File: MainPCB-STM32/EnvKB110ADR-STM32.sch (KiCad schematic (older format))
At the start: 246 parts, among them SW1 Boot Mode, SW2 Reset Switch, U1 XC6206PxxxMR, U2 STM32F411CEUx, Y1 3225_4P 32.768khz

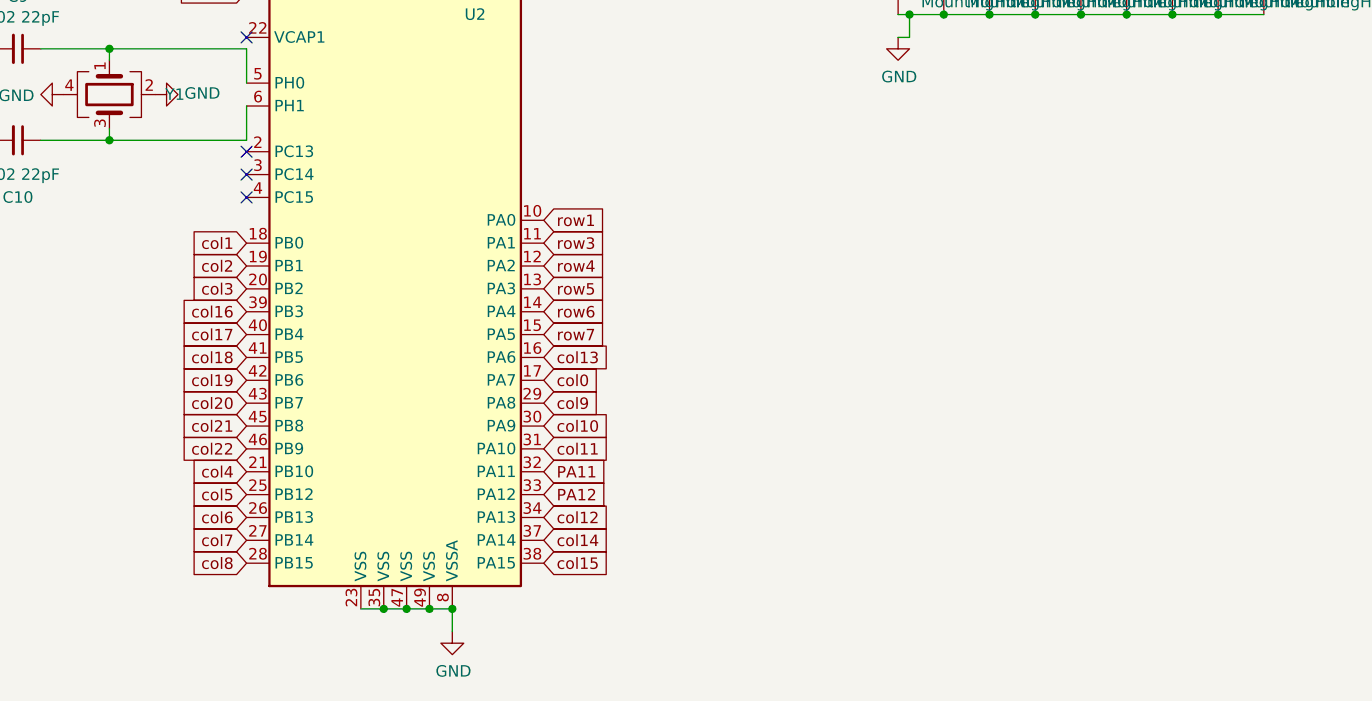
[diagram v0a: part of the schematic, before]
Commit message: Flipped STM32 to other side of board and added a debug header (SWDIO/SWCLK)
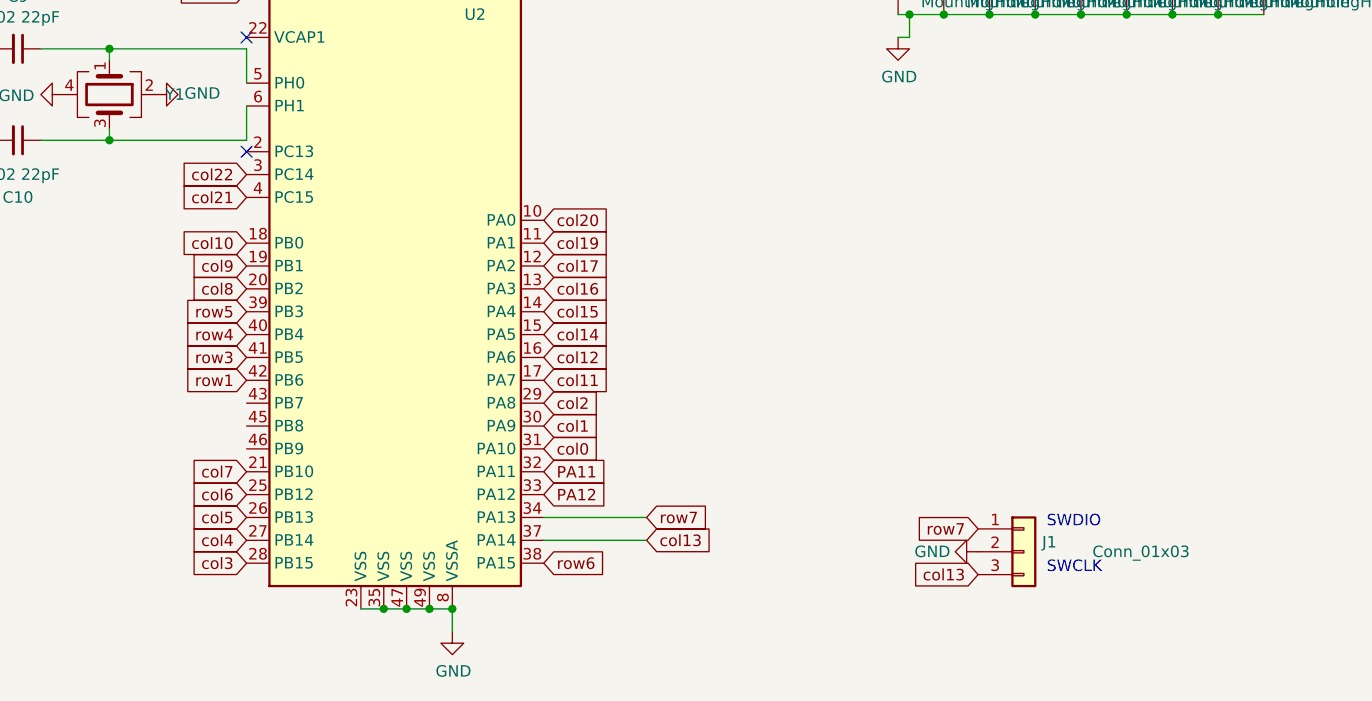
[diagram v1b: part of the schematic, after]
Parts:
- added J1: Conn_01x03, Connector_PinSocket_2.54mm:PinSocket_1x03_P2.54mm_Horizontal, symbol Connector_Generic:Conn_01x03
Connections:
- net col18 is gone; now on net row3: U2.41 (PB5)
- net GND: now also J1.2 (Pin_2)
- net col0: now also U2.31 (PA10); no longer U2.17 (PA7)
- net col1: now also U2.30 (PA9); no longer U2.18 (PB0)
- net col10: now also U2.18 (PB0); no longer U2.30 (PA9)
- net col11: now also U2.17 (PA7); no longer U2.31 (PA10)
- net col12: now also U2.16 (PA6); no longer U2.34 (PA13)
- net col13: now also U2.37 (PA14), J1.3 (Pin_3); no longer U2.16 (PA6)
- net col14: now also U2.15 (PA5); no longer U2.37 (PA14)
- net col15: now also U2.14 (PA4); no longer U2.38 (PA15)
- net col16: now also U2.13 (PA3); no longer U2.39 (PB3)
- net col17: now also U2.12 (PA2); no longer U2.40 (PB4)
- net col19: now also U2.11 (PA1); no longer U2.42 (PB6)
- net col2: now also U2.29 (PA8); no longer U2.19 (PB1)
- net col20: now also U2.10 (PA0); no longer U2.43 (PB7)
- net col21: now also U2.4 (PC15); no longer U2.45 (PB8)
- net col22: now also U2.3 (PC14); no longer U2.46 (PB9)
- net col3: now also U2.28 (PB15); no longer U2.20 (PB2)
- net col4: now also U2.27 (PB14); no longer U2.21 (PB10)
- net col5: now also U2.26 (PB13); no longer U2.25 (PB12)
- net col6: now also U2.25 (PB12); no longer U2.26 (PB13)
- net col7: now also U2.21 (PB10); no longer U2.27 (PB14)
- net col8: now also U2.20 (PB2); no longer U2.28 (PB15)
- net col9: now also U2.19 (PB1); no longer U2.29 (PA8)
- net row1: now also U2.42 (PB6); no longer U2.10 (PA0)
- net row3: no longer U2.11 (PA1)
- net row4: now also U2.40 (PB4); no longer U2.12 (PA2)
- net row5: now also U2.39 (PB3); no longer U2.13 (PA3)
- net row6: now also U2.38 (PA15); no longer U2.14 (PA4)
- net row7: now also U2.34 (PA13), J1.1 (Pin_1); no longer U2.15 (PA5)
- no-connect marks 7 -> 5
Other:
- note added: "SWCLK"
- note added: "SWDIO"
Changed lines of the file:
@@
 	1    0    0    -1
 $EndComp
+Text GLabel 14000 12250 2    50   Input ~ 0
+col0
+Text GLabel 14000 12150 2    50   Input ~ 0
+col1
+Text GLabel 14000 12050 2    50   Input ~ 0
+col2
+Text GLabel 12700 12750 0    50   Input ~ 0
+col3
+Text GLabel 12700 12650 0    50   Input ~ 0
+col4
+Text GLabel 12700 12550 0    50   Input ~ 0
+col5
+Text GLabel 12700 12450 0    50   Input ~ 0
+col6
+Text GLabel 12700 12350 0    50   Input ~ 0
+col7
+Text GLabel 12700 11550 0    50   Input ~ 0
+col8
+Text GLabel 12700 11450 0    50   Input ~ 0
+col9
+Text GLabel 12700 11350 0    50   Input ~ 0
+col10
 Text GLabel 14000 11950 2    50   Input ~ 0
-col0
-Text GLabel 12700 11350 0    50   Input ~ 0
-col1
-Text GLabel 12700 11450 0    50   Input ~ 0
-col2
-Text GLabel 12700 11550 0    50   Input ~ 0
-col3
-Text GLabel 12700 12350 0    50   Input ~ 0
-col4
-Text GLabel 12700 12450 0    50   Input ~ 0
-col5
-Text GLabel 12700 12550 0    50   Input ~ 0
-col6
-Text GLabel 12700 12650 0    50   Input ~ 0
-col7
-Text GLabel 12700 12750 0    50   Input ~ 0
-col8
-Text GLabel 14000 12050 2    50   Input ~ 0
-col9
-Text GLabel 14000 12150 2    50   Input ~ 0
-col10
-Text GLabel 14000 12250 2    50   Input ~ 0
 col11
-Text GLabel 14000 12550 2    50   Input ~ 0
+Text GLabel 14000 11850 2    50   Input ~ 0
 col12
-Text GLabel 14000 11850 2    50   Input ~ 0
+Text GLabel 14450 12650 2    50   Input ~ 0
 col13
-Text GLabel 14000 12650 2    50   Input ~ 0
+Text GLabel 14000 11750 2    50   Input ~ 0
 col14
+Text GLabel 14000 11650 2    50   Input ~ 0
+col15
+Text GLabel 14000 11550 2    50   Input ~ 0
+col16
+Text GLabel 14000 11450 2    50   Input ~ 0
+col17
+Text GLabel 14000 11350 2    50   Input ~ 0
+col19
+Text GLabel 14000 11250 2    50   Input ~ 0
+col20
+Text GLabel 12700 11150 0    50   Input ~ 0
+col21
+Text GLabel 12700 11050 0    50   Input ~ 0
+col22
+Text GLabel 12700 11950 0    50   Input ~ 0
+row1
+Text GLabel 12700 11850 0    50   Input ~ 0
+row3
+Text GLabel 12700 11750 0    50   Input ~ 0
+row4
+Text GLabel 12700 11650 0    50   Input ~ 0
+row5
 Text GLabel 14000 12750 2    50   Input ~ 0
-col15
-Text GLabel 12700 11650 0    50   Input ~ 0
-col16
-Text GLabel 12700 11750 0    50   Input ~ 0
-col17
-Text GLabel 12700 11850 0    50   Input ~ 0
-col18
-Text GLabel 12700 11950 0    50   Input ~ 0
-col19
-Text GLabel 12700 12050 0    50   Input ~ 0
-col20
-Text GLabel 12700 12150 0    50   Input ~ 0
-col21
-Text GLabel 12700 12250 0    50   Input ~ 0
-col22
-Text GLabel 14000 11250 2    50   Input ~ 0
-row1
-Text GLabel 14000 11350 2    50   Input ~ 0
-row3
-Text GLabel 14000 11450 2    50   Input ~ 0
-row4
-Text GLabel 14000 11550 2    50   Input ~ 0
-row5
-Text GLabel 14000 11650 2    50   Input ~ 0
 row6
-Text GLabel 14000 11750 2    50   Input ~ 0
+Text GLabel 14450 12550 2    50   Input ~ 0
 row7
 Wire Wire Line
@@
 Connection ~ 12100 10500
 $Comp
+L Device:C_Small C9
+U 1 1 616BF174
+P 11700 10500
+F 0 "C9" V 11929 10500 50  0000 C CNN
+F 1 "0402 22pF" V 11838 10500 50  0000 C CNN
+F 2 "Capacitor_SMD:C_0402_1005Metric" H 11700 10500 50  0001 C CNN
+F 3 "~" H 11700 10500 50  0001 C CNN
+	1    11700 10500
+	0    1    -1   0
+$EndComp
+$Comp
+L power:GND #PWR0118
+U 1 1 616C0646
+P 11900 10700
+F 0 "#PWR0118" H 11900 10450 50  0001 C CNN
+F 1 "GND" V 11905 10572 50  0000 R CNN
+F 2 "" H 11900 10700 50  0001 C CNN
+F 3 "" H 11900 10700 50  0001 C CNN
+	1    11900 10700
+	0    1    1    0
+$EndComp
+$Comp
+L power:GND #PWR0119
+U 1 1 616C18A1
+P 12300 10700
+F 0 "#PWR0119" H 12300 10450 50  0001 C CNN
+F 1 "GND" V 12305 10572 50  0000 R CNN
+F 2 "" H 12300 10700 50  0001 C CNN
+F 3 "" H 12300 10700 50  0001 C CNN
+	1    12300 10700
+	0    -1   -1   0
+$EndComp
+$Comp
+L power:GND #PWR0120
+U 1 1 616C1C2C
+P 11500 10700
+F 0 "#PWR0120" H 11500 10450 50  0001 C CNN
+F 1 "GND" V 11505 10572 50  0000 R CNN
+F 2 "" H 11500 10700 50  0001 C CNN
+F 3 "" H 11500 10700 50  0001 C CNN
+	1    11500 10700
+	0    1    1    0
+$EndComp
+Wire Wire Line
+	12700 10900 12100 10900
+Wire Wire Line
+	12100 10900 12100 10850
+Wire Wire Line
+	12100 10900 11800 10900
+Connection ~ 12100 10900
+Wire Wire Line
+	12700 10750 12700 10900
+Wire Wire Line
+	11600 10900 11600 10700
+Wire Wire Line
+	11600 10700 11500 10700
+Wire Wire Line
+	11600 10700 11600 10500
+Connection ~ 11600 10700
+NoConn ~ 12700 10950
+NoConn ~ 9550 11150
+NoConn ~ 9550 10550
+Wire Wire Line
+	9550 11450 9550 11550
+Connection ~ 9550 11550
+Wire Wire Line
+	9550 11550 9550 11650
+$Comp
 L Device:C_Small C10
 U 1 1 616BE7BD
@@
 	0    1    -1   0
 $EndComp
-$Comp
-L Device:C_Small C9
-U 1 1 616BF174
-P 11700 10500
-F 0 "C9" V 11929 10500 50  0000 C CNN
-F 1 "0402 22pF" V 11838 10500 50  0000 C CNN
-F 2 "Capacitor_SMD:C_0402_1005Metric" H 11700 10500 50  0001 C CNN
-F 3 "~" H 11700 10500 50  0001 C CNN
-	1    11700 10500
-	0    1    -1   0
-$EndComp
-$Comp
-L power:GND #PWR0118
-U 1 1 616C0646
-P 11900 10700
-F 0 "#PWR0118" H 11900 10450 50  0001 C CNN
-F 1 "GND" V 11905 10572 50  0000 R CNN
-F 2 "" H 11900 10700 50  0001 C CNN
-F 3 "" H 11900 10700 50  0001 C CNN
-	1    11900 10700
+Wire Wire Line
+	14000 12550 14450 12550
+Wire Wire Line
+	14000 12650 14450 12650
+$Comp
+L power:GND #PWR0121
+U 1 1 61D38795
+P 15900 12700
+F 0 "#PWR0121" H 15900 12450 50  0001 C CNN
+F 1 "GND" V 15900 12500 50  0000 C CNN
+F 2 "" H 15900 12700 50  0001 C CNN
+F 3 "" H 15900 12700 50  0001 C CNN
+	1    15900 12700
 	0    1    1    0
 $EndComp
-$Comp
-L power:GND #PWR0119
-U 1 1 616C18A1
-P 12300 10700
-F 0 "#PWR0119" H 12300 10450 50  0001 C CNN
-F 1 "GND" V 12305 10572 50  0000 R CNN
-F 2 "" H 12300 10700 50  0001 C CNN
-F 3 "" H 12300 10700 50  0001 C CNN
-	1    12300 10700
-	0    -1   -1   0
-$EndComp
-$Comp
-L power:GND #PWR0120
-U 1 1 616C1C2C
-P 11500 10700
-F 0 "#PWR0120" H 11500 10450 50  0001 C CNN
-F 1 "GND" V 11505 10572 50  0000 R CNN
-F 2 "" H 11500 10700 50  0001 C CNN
-F 3 "" H 11500 10700 50  0001 C CNN
-	1    11500 10700
-	0    1    1    0
-$EndComp
-Wire Wire Line
-	12700 10900 12100 10900
-Wire Wire Line
-	12100 10900 12100 10850
-Wire Wire Line
-	12100 10900 11800 10900
-Connection ~ 12100 10900
-Wire Wire Line
-	12700 10750 12700 10900
-Wire Wire Line
-	11600 10900 11600 10700
-Wire Wire Line
-	11600 10700 11500 10700
-Wire Wire Line
-	11600 10700 11600 10500
-Connection ~ 11600 10700
-NoConn ~ 12700 10950
-NoConn ~ 12700 11050
-NoConn ~ 12700 11150
-NoConn ~ 9550 11150
-NoConn ~ 9550 10550
-Wire Wire Line
-	9550 11450 9550 11550
-Connection ~ 9550 11550
-Wire Wire Line
-	9550 11550 9550 11650
+Text GLabel 15900 12800 0    50   Input ~ 0
+col13
+Text GLabel 15900 12600 0    50   Input ~ 0
+row7
+Text Notes 16200 12600 0    50   ~ 0
+SWDIO
+Text Notes 16200 12800 0    50   ~ 0
+SWCLK
+$Comp
+L Connector_Generic:Conn_01x03 J1
+U 1 1 61D3730E
+P 16100 12700
+F 0 "J1" H 16180 12742 50  0000 L CNN
+F 1 "Conn_01x03" H 16400 12700 50  0000 L CNN
+F 2 "Connector_PinSocket_2.54mm:PinSocket_1x03_P2.54mm_Horizontal" H 16100 12700 50  0001 C CNN
+F 3 "~" H 16100 12700 50  0001 C CNN
+	1    16100 12700
+	1    0    0    -1
+$EndComp
 $EndSCHEMATC

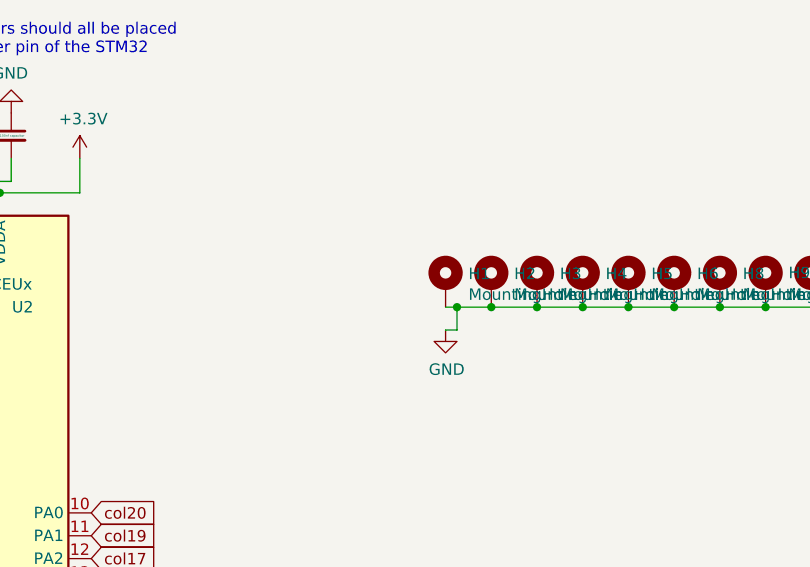
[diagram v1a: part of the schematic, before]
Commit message: added mount holes, fixed a couple trace errors, created backplate PCB
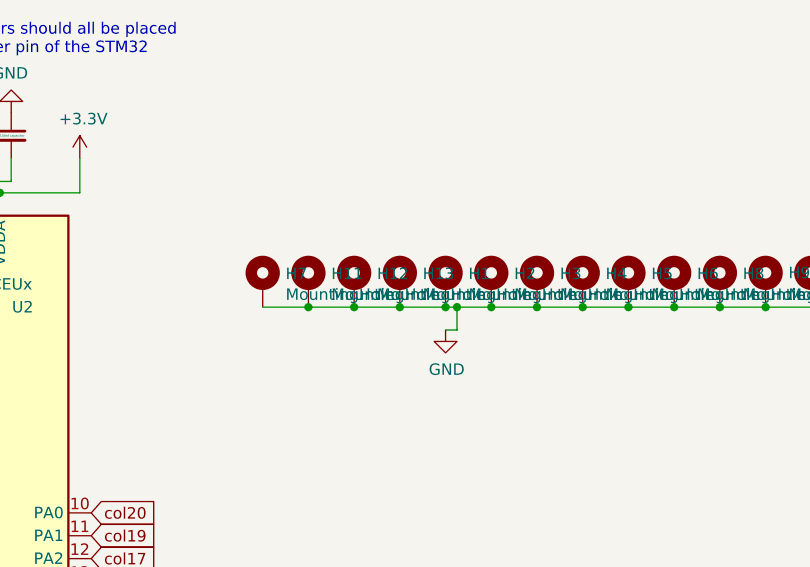
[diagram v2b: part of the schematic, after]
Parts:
- added H11, H12, H13, H7: MountingHole, MountingHole:MountingHole_2.2mm_M2_Pad, symbol Mechanical:MountingHole_Pad
- H1, H10, H2, H3, H4, H5, H6, H8, H9: footprint MountingHole:MountingHole_2.2mm_M2 -> MountingHole:MountingHole_2.2mm_M2_Pad
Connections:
- net GND: now also H11.1, H12.1, H13.1, H7.1
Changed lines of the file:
@@
 F 0 "H1" H 15650 10296 50  0000 L CNN
 F 1 "MountingHole" H 15650 10205 50  0000 L CNN
-F 2 "MountingHole:MountingHole_2.2mm_M2" H 15550 10250 50  0001 C CNN
+F 2 "MountingHole:MountingHole_2.2mm_M2_Pad" H 15550 10250 50  0001 C CNN
 F 3 "~" H 15550 10250 50  0001 C CNN
 	1    15550 10250
@@
 F 0 "H2" H 15850 10296 50  0000 L CNN
 F 1 "MountingHole" H 15850 10205 50  0000 L CNN
-F 2 "MountingHole:MountingHole_2.2mm_M2" H 15750 10250 50  0001 C CNN
+F 2 "MountingHole:MountingHole_2.2mm_M2_Pad" H 15750 10250 50  0001 C CNN
 F 3 "~" H 15750 10250 50  0001 C CNN
 	1    15750 10250
@@
 F 0 "H3" H 16050 10296 50  0000 L CNN
 F 1 "MountingHole" H 16050 10205 50  0000 L CNN
-F 2 "MountingHole:MountingHole_2.2mm_M2" H 15950 10250 50  0001 C CNN
+F 2 "MountingHole:MountingHole_2.2mm_M2_Pad" H 15950 10250 50  0001 C CNN
 F 3 "~" H 15950 10250 50  0001 C CNN
 	1    15950 10250
@@
 F 0 "H4" H 16250 10296 50  0000 L CNN
 F 1 "MountingHole" H 16250 10205 50  0000 L CNN
-F 2 "MountingHole:MountingHole_2.2mm_M2" H 16150 10250 50  0001 C CNN
+F 2 "MountingHole:MountingHole_2.2mm_M2_Pad" H 16150 10250 50  0001 C CNN
 F 3 "~" H 16150 10250 50  0001 C CNN
 	1    16150 10250
@@
 F 0 "H5" H 16450 10296 50  0000 L CNN
 F 1 "MountingHole" H 16450 10205 50  0000 L CNN
-F 2 "MountingHole:MountingHole_2.2mm_M2" H 16350 10250 50  0001 C CNN
+F 2 "MountingHole:MountingHole_2.2mm_M2_Pad" H 16350 10250 50  0001 C CNN
 F 3 "~" H 16350 10250 50  0001 C CNN
 	1    16350 10250
@@
 F 0 "H6" H 16650 10296 50  0000 L CNN
 F 1 "MountingHole" H 16650 10205 50  0000 L CNN
-F 2 "MountingHole:MountingHole_2.2mm_M2" H 16550 10250 50  0001 C CNN
+F 2 "MountingHole:MountingHole_2.2mm_M2_Pad" H 16550 10250 50  0001 C CNN
 F 3 "~" H 16550 10250 50  0001 C CNN
 	1    16550 10250
@@
 F 0 "H8" H 16850 10296 50  0000 L CNN
 F 1 "MountingHole" H 16850 10205 50  0000 L CNN
-F 2 "MountingHole:MountingHole_2.2mm_M2" H 16750 10250 50  0001 C CNN
+F 2 "MountingHole:MountingHole_2.2mm_M2_Pad" H 16750 10250 50  0001 C CNN
 F 3 "~" H 16750 10250 50  0001 C CNN
 	1    16750 10250
@@
 F 0 "H9" H 17050 10300 50  0000 L CNN
 F 1 "MountingHole" H 17050 10205 50  0000 L CNN
-F 2 "MountingHole:MountingHole_2.2mm_M2" H 16950 10250 50  0001 C CNN
+F 2 "MountingHole:MountingHole_2.2mm_M2_Pad" H 16950 10250 50  0001 C CNN
 F 3 "~" H 16950 10250 50  0001 C CNN
 	1    16950 10250
@@
 F 0 "H10" H 17250 10296 50  0000 L CNN
 F 1 "MountingHole" H 17250 10205 50  0000 L CNN
-F 2 "MountingHole:MountingHole_2.2mm_M2" H 17150 10250 50  0001 C CNN
+F 2 "MountingHole:MountingHole_2.2mm_M2_Pad" H 17150 10250 50  0001 C CNN
 F 3 "~" H 17150 10250 50  0001 C CNN
 	1    17150 10250
@@
 	1    0    0    -1
 $EndComp
+$Comp
+L Mechanical:MountingHole_Pad H13
+U 1 1 6159BEF9
+P 15350 10250
+F 0 "H13" H 15450 10296 50  0000 L CNN
+F 1 "MountingHole" H 15450 10205 50  0000 L CNN
+F 2 "MountingHole:MountingHole_2.2mm_M2_Pad" H 15350 10250 50  0001 C CNN
+F 3 "~" H 15350 10250 50  0001 C CNN
+	1    15350 10250
+	1    0    0    -1
+$EndComp
+$Comp
+L Mechanical:MountingHole_Pad H12
+U 1 1 6159C0F0
+P 15150 10250
+F 0 "H12" H 15250 10296 50  0000 L CNN
+F 1 "MountingHole" H 15250 10205 50  0000 L CNN
+F 2 "MountingHole:MountingHole_2.2mm_M2_Pad" H 15150 10250 50  0001 C CNN
+F 3 "~" H 15150 10250 50  0001 C CNN
+	1    15150 10250
+	1    0    0    -1
+$EndComp
+$Comp
+L Mechanical:MountingHole_Pad H11
+U 1 1 6159C37F
+P 14950 10250
+F 0 "H11" H 15050 10296 50  0000 L CNN
+F 1 "MountingHole" H 15050 10205 50  0000 L CNN
+F 2 "MountingHole:MountingHole_2.2mm_M2_Pad" H 14950 10250 50  0001 C CNN
+F 3 "~" H 14950 10250 50  0001 C CNN
+	1    14950 10250
+	1    0    0    -1
+$EndComp
+$Comp
+L Mechanical:MountingHole_Pad H7
+U 1 1 6159C5EF
+P 14750 10250
+F 0 "H7" H 14850 10296 50  0000 L CNN
+F 1 "MountingHole" H 14850 10205 50  0000 L CNN
+F 2 "MountingHole:MountingHole_2.2mm_M2_Pad" H 14750 10250 50  0001 C CNN
+F 3 "~" H 14750 10250 50  0001 C CNN
+	1    14750 10250
+	1    0    0    -1
+$EndComp
+Wire Wire Line
+	14750 10350 14950 10350
+Connection ~ 15550 10350
+Connection ~ 14950 10350
+Wire Wire Line
+	14950 10350 15150 10350
+Connection ~ 15150 10350
+Wire Wire Line
+	15150 10350 15350 10350
+Connection ~ 15350 10350
+Wire Wire Line
+	15350 10350 15550 10350
 $EndSCHEMATC
